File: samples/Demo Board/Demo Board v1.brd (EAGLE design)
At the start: 88.9 x 50.8 mm, 56 parts

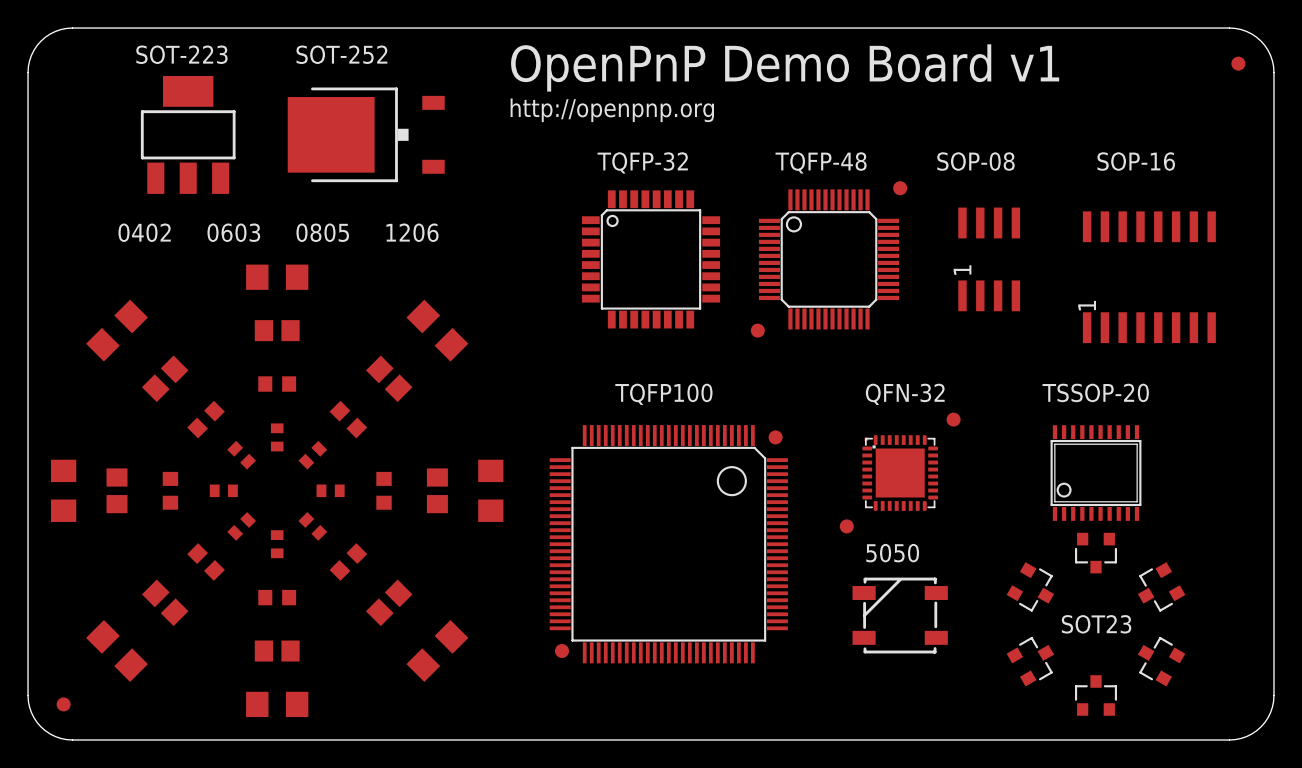
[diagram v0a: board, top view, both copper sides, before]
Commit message: Revert "Merge remote-tracking branch 'openpnp/feature/bottom-vision' into develop"
This reverts commit ee636cd801bb34ac247e5c3738f2d56de49d13b9, reversing
changes made to bc52f84d9261bfcd659cbfa6d23c96068bc62b4f.
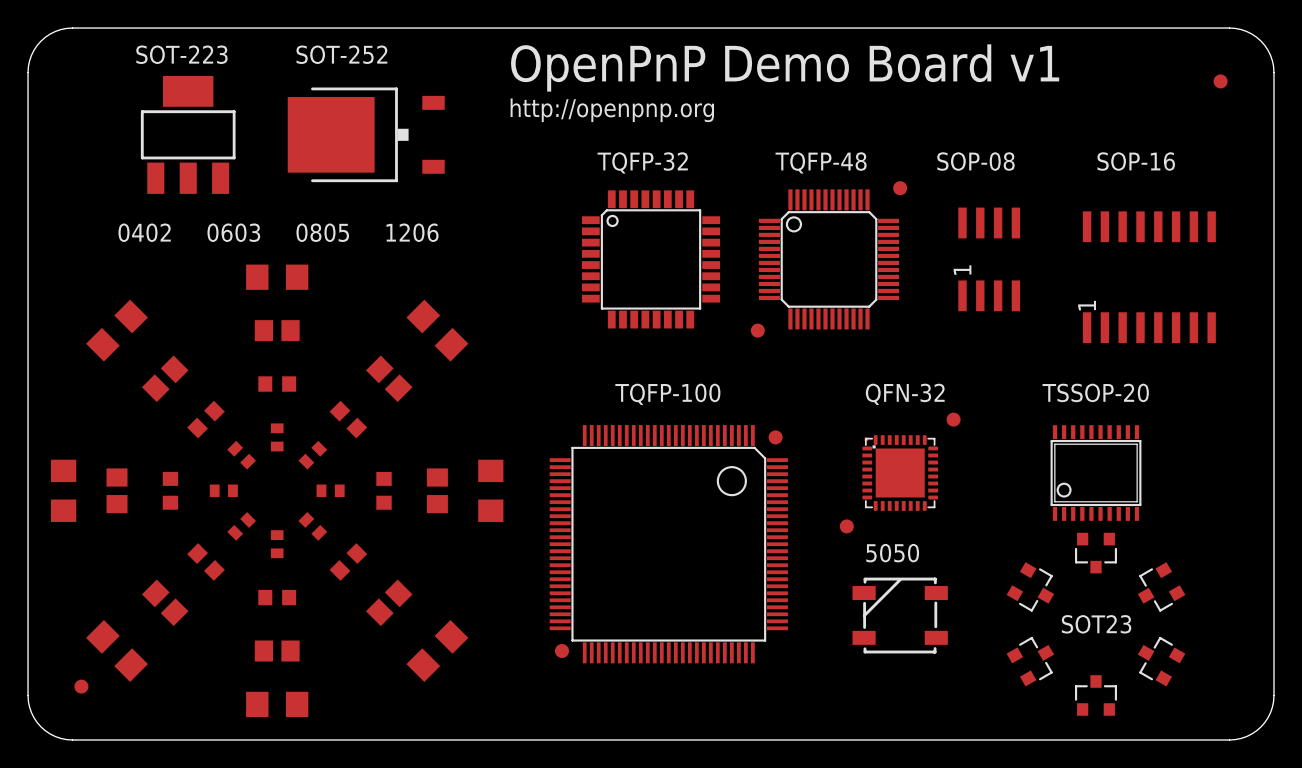
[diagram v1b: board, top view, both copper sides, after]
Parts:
- removed E$13, E$22: (no value), SparkFun-Aesthetics:FIDUCIAL-1X2
- added FID-1, FID-2: (no value), SparkFun-Aesthetics:FIDUCIAL-1X2
- renumbered E$1 to 5050, E$10 to TSSOP-20, E$11 to TQFP-32, E$12 to TQFP-48, E$14 to FID-5, E$15 to FID-6, E$16 to TQFP-100, E$17 to FID-3, E$18 to FID-4, E$19 to FID-7, E$2 to R1206-3, E$20 to FID-8, E$23 to R0402-1, E$24 to R0402-3, E$25 to R0402-5, E$26 to R0402-7, E$27 to R0402-2, E$28 to R0402-6, E$29 to R0402-8, E$3 to R1206-5, E$30 to R0402-4, E$31 to R0603-1, E$34 to R0603-5, E$35 to R0603-3, E$36 to R0603-7, E$37 to R0603-2, E$38 to R0603-4, E$39 to R0603-6, E$4 to SOP-16, E$40 to R0603-8, E$41 to R0805-1, E$42 to QFN-32, E$44 to R0805-3, E$45 to R0805-5, E$46 to R0805-7, E$47 to R0805-8, E$48 to R0805-6, E$5 to R1206-7, E$51 to SOT-223, E$52 to SOT-252, E$53 to SOP-08, E$54 to R0805-4, E$55 to R0805-2, E$56 to SOT-23-5, E$57 to SOT-23-6, E$58 to SOT-23-2, E$6 to R1206-8, E$60 to SOT-23-1, E$61 to SOT-23-4, E$62 to SOT-23-3, E$7 to R1206-2, E$8 to R1206-4, E$82 to R1206-1, E$9 to R1206-6
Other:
- board text added: "* FIDS are missing keepout"
- board text added: "TQFP-100"
- board text removed: "TQFP100"

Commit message: Revert "Revert "Merge remote-tracking branch 'openpnp/feature/bottom-vision' into develop""
This reverts commit 273c0c9d88a1beb8fff937c1a99141638172fa66.
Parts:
- removed FID-1, FID-2: (no value), SparkFun-Aesthetics:FIDUCIAL-1X2
- added E$13, E$22: (no value), SparkFun-Aesthetics:FIDUCIAL-1X2
- renumbered 5050 to E$1, FID-3 to E$17, FID-4 to E$18, FID-5 to E$14, FID-6 to E$15, FID-7 to E$19, FID-8 to E$20, QFN-32 to E$42, R0402-1 to E$23, R0402-2 to E$27, R0402-3 to E$24, R0402-4 to E$30, R0402-5 to E$25, R0402-6 to E$28, R0402-7 to E$26, R0402-8 to E$29, R0603-1 to E$31, R0603-2 to E$37, R0603-3 to E$35, R0603-4 to E$38, R0603-5 to E$34, R0603-6 to E$39, R0603-7 to E$36, R0603-8 to E$40, R0805-1 to E$41, R0805-2 to E$55, R0805-3 to E$44, R0805-4 to E$54, R0805-5 to E$45, R0805-6 to E$48, R0805-7 to E$46, R0805-8 to E$47, R1206-1 to E$82, R1206-2 to E$7, R1206-3 to E$2, R1206-4 to E$8, R1206-5 to E$3, R1206-6 to E$9, R1206-7 to E$5, R1206-8 to E$6, SOP-08 to E$53, SOP-16 to E$4, SOT-223 to E$51, SOT-23-1 to E$60, SOT-23-2 to E$58, SOT-23-3 to E$62, SOT-23-4 to E$61, SOT-23-5 to E$56, SOT-23-6 to E$57, SOT-252 to E$52, TQFP-100 to E$16, TQFP-32 to E$11, TQFP-48 to E$12, TSSOP-20 to E$10
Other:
- board text added: "TQFP100"
- board text removed: "* FIDS are missing keepout"
- board text removed: "TQFP-100"
